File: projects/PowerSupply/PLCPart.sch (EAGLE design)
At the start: 30 parts, among them IC1 L7815CV, IC2 L7915CV, IC3 L7805CV, IC4 LM741P, IC5 LM741P, X1 SUPPLY-IN, X2 VCC-IN

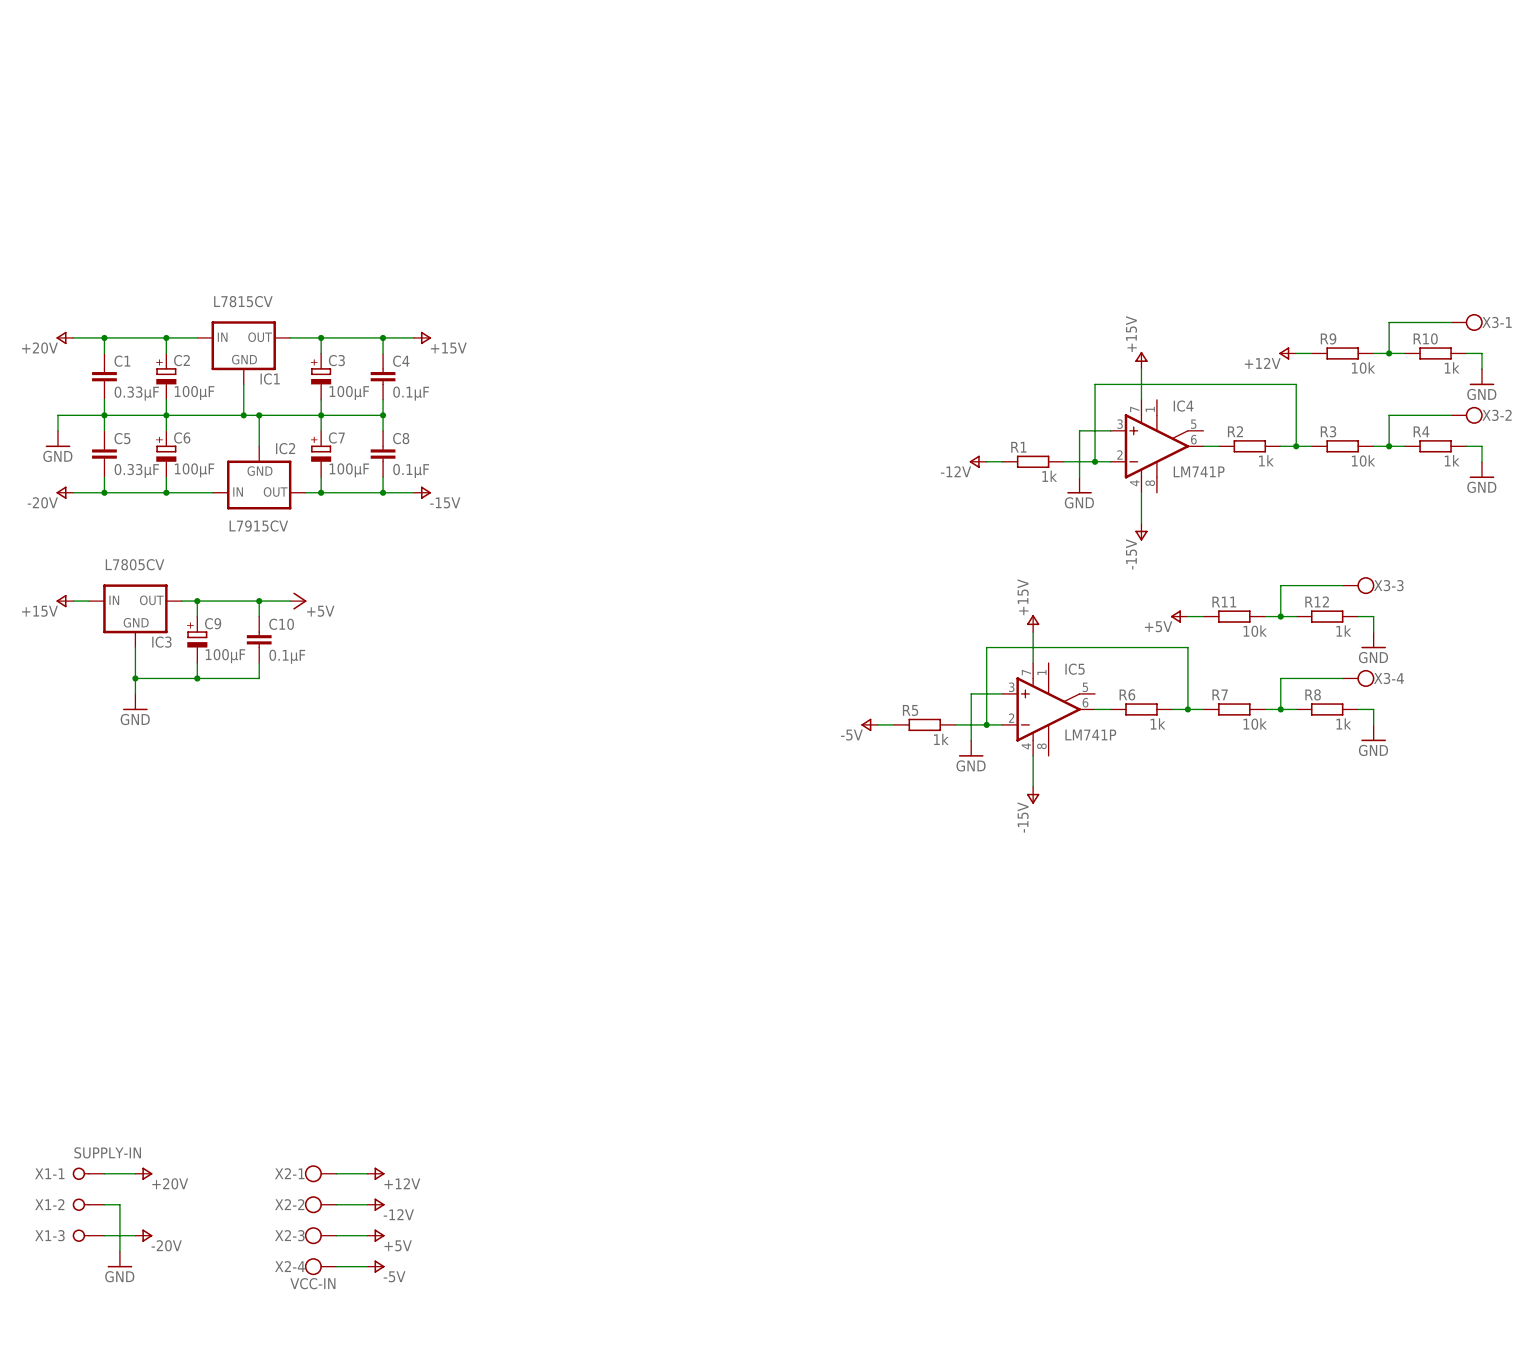
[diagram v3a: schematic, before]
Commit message: feat: plc part improved
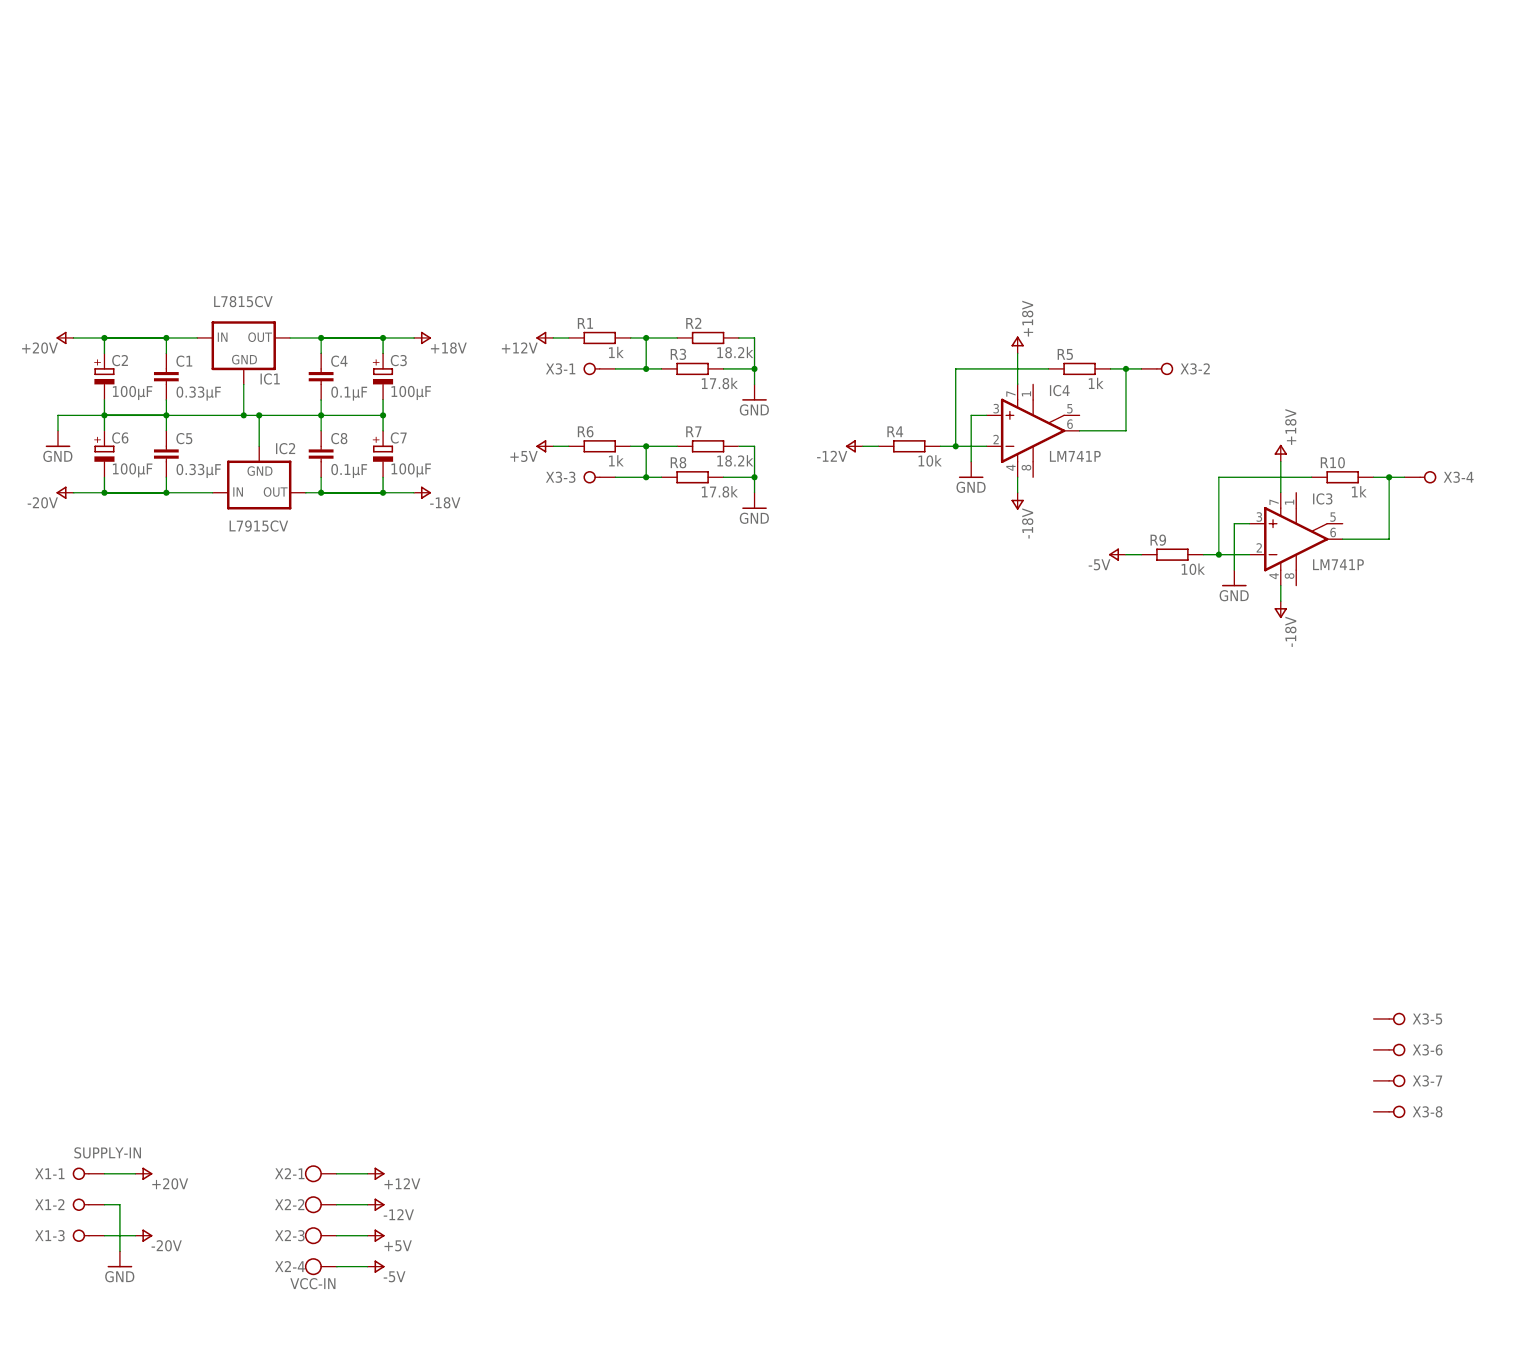
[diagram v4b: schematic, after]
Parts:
- removed C10: 0.1µF, rcl:C-EU050-024X044
- removed C9: 100µF, rcl:CPOL-EUE2.5-6
- removed IC5: LM741P, linear:LM741P
- removed R11: 10k, rcl:R-EU_0207/10
- removed R12: 1k, rcl:R-EU_0207/10
- IC3: value L7805CV -> LM741P; device v-reg:78XXS -> linear:LM741P
- R2: value 1k -> 18.2k
- R3: value 10k -> 17.8k
- R4: value 1k -> 10k
- R7: value 10k -> 18.2k
- R8: value 1k -> 17.8k
- X3: device con-wago-500:W237-4 -> con-wago-508:W237-08P
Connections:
- removed net +15V: C3.+, C4.1, IC1.OUT, IC3.IN, IC4.V+, IC5.V+
- removed net -15V: C7.-, C8.2, IC2.OUT, IC4.V-, IC5.V-
- removed net N$10: R11.2, R12.1, X3-3.KL
- removed net N$8: R10.1, R9.2, X3-1.KL
- new net +18V: C3.+, C4.1, IC1.OUT, IC3.V+, IC4.V+
- new net -18V: C7.-, C8.2, IC2.OUT, IC3.V-, IC4.V-
- net +12V: now also R1.1; no longer R9.1
- net +5V: now also R6.1; no longer C10.1, C9.+, IC3.OUT, R11.1
- net -12V: now also R4.1; no longer R1.1
- net -5V: now also R9.1; no longer R5.1
- net GND: now also IC3.+IN, R2.2, R3.2, R7.2; no longer C10.2, C9.-, IC3.GND, IC5.+IN, R10.2, R12.2, R4.2
- net N$1: now also R4.2, R5.1; no longer R1.2, R2.2, R3.1
- net N$2: now also IC4.OUT, R5.2; no longer R3.2, R4.1
- net N$3: now also IC3.-IN, R10.1, R9.2; no longer IC4.OUT, R2.1
- net N$4: now also R8.1, X3-3.KL; no longer IC5.-IN, R5.2
- net N$5: now also R1.2, R2.1, R3.1, X3-1.KL; no longer IC5.OUT, R6.1
- net N$6: now also IC3.OUT, R10.2; no longer R7.2, R8.1
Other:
- moved on the sheet: C1, C2, C3, C4, C5, C6, C7, C8, IC4, R1, R10, R2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

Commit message: feat: plc part small fixes applied
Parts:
- IC1: value L7815CV -> L7818CV
- IC2: value L7915CV -> L7918CV
- X1: value SUPPLY-IN -> MCU-PWR
- X2: value VCC-IN -> MCU-IN; device con-wago-500:W237-4 -> con-wago-508:W237-04P
- X3: value (none) -> MCU-OUT
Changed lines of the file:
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@@
 <parts>
 <part name="GND5" library="supply1" library_urn="urn:adsk.eagle:library:371" deviceset="GND" device=""/>
-<part name="X1" library="con-wago-508" library_urn="urn:adsk.eagle:library:196" deviceset="W237-03P" device="" package3d_urn="urn:adsk.eagle:package:10737/1" value="SUPPLY-IN"/>
+<part name="X1" library="con-wago-508" library_urn="urn:adsk.eagle:library:196" deviceset="W237-03P" device="" package3d_urn="urn:adsk.eagle:package:10737/1" value="MCU-PWR"/>
 <part name="P+4" library="bb84-supply" deviceset="+20V" device=""/>
 <part name="P-4" library="bb84-supply" deviceset="-20V" device=""/>
 <part name="FRAME1" library="frames" library_urn="urn:adsk.eagle:library:229" deviceset="A4L-LOC" device="" value="12VPart"/>
-<part name="IC2" library="v-reg" library_urn="urn:adsk.eagle:library:409" deviceset="79XXS" device="" package3d_urn="urn:adsk.eagle:package:30343/1" value="L7915CV"/>
-<part name="IC1" library="v-reg" library_urn="urn:adsk.eagle:library:409" deviceset="78XXS" device="" package3d_urn="urn:adsk.eagle:package:30342/1" value="L7815CV"/>
+<part name="IC2" library="v-reg" library_urn="urn:adsk.eagle:library:409" deviceset="79XXS" device="" package3d_urn="urn:adsk.eagle:package:30343/1" value="L7918CV"/>
+<part name="IC1" library="v-reg" library_urn="urn:adsk.eagle:library:409" deviceset="78XXS" device="" package3d_urn="urn:adsk.eagle:package:30342/1" value="L7818CV"/>
 <part name="P+1" library="bb84-supply" deviceset="+20V" device=""/>
 <part name="P-1" library="bb84-supply" deviceset="-20V" device=""/>
@@
 <part name="C6" library="rcl" library_urn="urn:adsk.eagle:library:334" deviceset="CPOL-EU" device="E2.5-6" package3d_urn="urn:adsk.eagle:package:23349/1" value="100µF"/>
 <part name="C7" library="rcl" library_urn="urn:adsk.eagle:library:334" deviceset="CPOL-EU" device="E2.5-6" package3d_urn="urn:adsk.eagle:package:23349/1" value="100µF"/>
-<part name="X2" library="con-wago-500" library_urn="urn:adsk.eagle:library:195" deviceset="W237-4" device="" package3d_urn="urn:adsk.eagle:package:10695/1" value="VCC-IN"/>
 <part name="P+6" library="bb84-supply" deviceset="+12V" device=""/>
 <part name="P-3" library="bb84-supply" deviceset="-12V" device=""/>
@@
 <part name="P+3" library="bb84-supply" deviceset="+18V" device=""/>
 <part name="P-6" library="bb84-supply" deviceset="-18V" device=""/>
-<part name="X3" library="con-wago-508" library_urn="urn:adsk.eagle:library:196" deviceset="W237-08P" device="" package3d_urn="urn:adsk.eagle:package:10738/1"/>
+<part name="X3" library="con-wago-508" library_urn="urn:adsk.eagle:library:196" deviceset="W237-08P" device="" package3d_urn="urn:adsk.eagle:package:10738/1" value="MCU-OUT"/>
 <part name="P+8" library="bb84-supply" deviceset="+12V" device=""/>
 <part name="R1" library="rcl" library_urn="urn:adsk.eagle:library:334" deviceset="R-EU_" device="0207/10" package3d_urn="urn:adsk.eagle:package:23491/2" value="1k"/>
@@
 <part name="P+9" library="bb84-supply" deviceset="+5V" device=""/>
 <part name="P-8" library="bb84-supply" deviceset="-5V" device=""/>
+<part name="X2" library="con-wago-508" library_urn="urn:adsk.eagle:library:196" deviceset="W237-04P" device="" package3d_urn="urn:adsk.eagle:package:10735/1" value="MCU-IN"/>
 </parts>
 <sheets>
@@
 <attribute name="VALUE" x="69.723" y="145.2626" size="1.778" layer="96"/>
 </instance>
-<instance part="X2" gate="-1" x="55.88" y="30.48" smashed="yes">
-<attribute name="NAME" x="55.88" y="31.369" size="1.778" layer="95" rot="R180"/>
-</instance>
-<instance part="X2" gate="-2" x="55.88" y="25.4" smashed="yes">
-<attribute name="NAME" x="55.88" y="26.289" size="1.778" layer="95" rot="R180"/>
-</instance>
-<instance part="X2" gate="-3" x="55.88" y="20.32" smashed="yes">
-<attribute name="NAME" x="55.88" y="21.209" size="1.778" layer="95" rot="R180"/>
-</instance>
-<instance part="X2" gate="-4" x="55.88" y="15.24" smashed="yes">
-<attribute name="VALUE" x="53.34" y="11.557" size="1.778" layer="96"/>
-<attribute name="NAME" x="55.88" y="16.129" size="1.778" layer="95" rot="R180"/>
-</instance>
 <instance part="P+6" gate="G$1" x="68.58" y="30.48" smashed="yes" rot="R270">
 <attribute name="VALUE" x="68.58" y="27.94" size="1.778" layer="96"/>
@@
 <instance part="P-8" gate="G$1" x="187.96" y="132.08" smashed="yes" rot="MR90">
 <attribute name="VALUE" x="187.96" y="129.54" size="1.778" layer="96" rot="MR0"/>
+</instance>
+<instance part="X2" gate="-1" x="55.88" y="30.48" smashed="yes">
+<attribute name="NAME" x="54.61" y="31.369" size="1.778" layer="95" rot="R180"/>
+</instance>
+<instance part="X2" gate="-2" x="55.88" y="25.4" smashed="yes">
+<attribute name="NAME" x="54.61" y="26.289" size="1.778" layer="95" rot="R180"/>
+</instance>
+<instance part="X2" gate="-3" x="55.88" y="20.32" smashed="yes">
+<attribute name="NAME" x="54.61" y="21.209" size="1.778" layer="95" rot="R180"/>
+</instance>
+<instance part="X2" gate="-4" x="55.88" y="15.24" smashed="yes">
+<attribute name="VALUE" x="55.88" y="33.02" size="1.778" layer="96"/>
+<attribute name="NAME" x="54.61" y="16.129" size="1.778" layer="95" rot="R180"/>
 </instance>
 </instances>
@@
 <net name="+5V" class="0">
 <segment>
-<pinref part="X2" gate="-3" pin="KL"/>
 <pinref part="P+7" gate="G$1" pin="+5V"/>
 <wire x1="60.96" y1="20.32" x2="66.04" y2="20.32" width="0.1524" layer="91"/>
+<pinref part="X2" gate="-3" pin="KL"/>
 </segment>
 <segment>
@@
 <net name="+12V" class="0">
 <segment>
-<pinref part="X2" gate="-1" pin="KL"/>
 <pinref part="P+6" gate="G$1" pin="+12V"/>
 <wire x1="60.96" y1="30.48" x2="66.04" y2="30.48" width="0.1524" layer="91"/>
+<pinref part="X2" gate="-1" pin="KL"/>
 </segment>
 <segment>
@@
 <segment>
 <pinref part="P-3" gate="G$1" pin="-12V"/>
+<wire x1="66.04" y1="25.4" x2="60.96" y2="25.4" width="0.1524" layer="91"/>
 <pinref part="X2" gate="-2" pin="KL"/>
-<wire x1="66.04" y1="25.4" x2="60.96" y2="25.4" width="0.1524" layer="91"/>
 </segment>
 <segment>
@@
 <segment>
 <pinref part="P-5" gate="G$1" pin="-5V"/>
+<wire x1="66.04" y1="15.24" x2="60.96" y2="15.24" width="0.1524" layer="91"/>
 <pinref part="X2" gate="-4" pin="KL"/>
-<wire x1="66.04" y1="15.24" x2="60.96" y2="15.24" width="0.1524" layer="91"/>
-</segment>
-<segment>
+</segment>
+<segment>

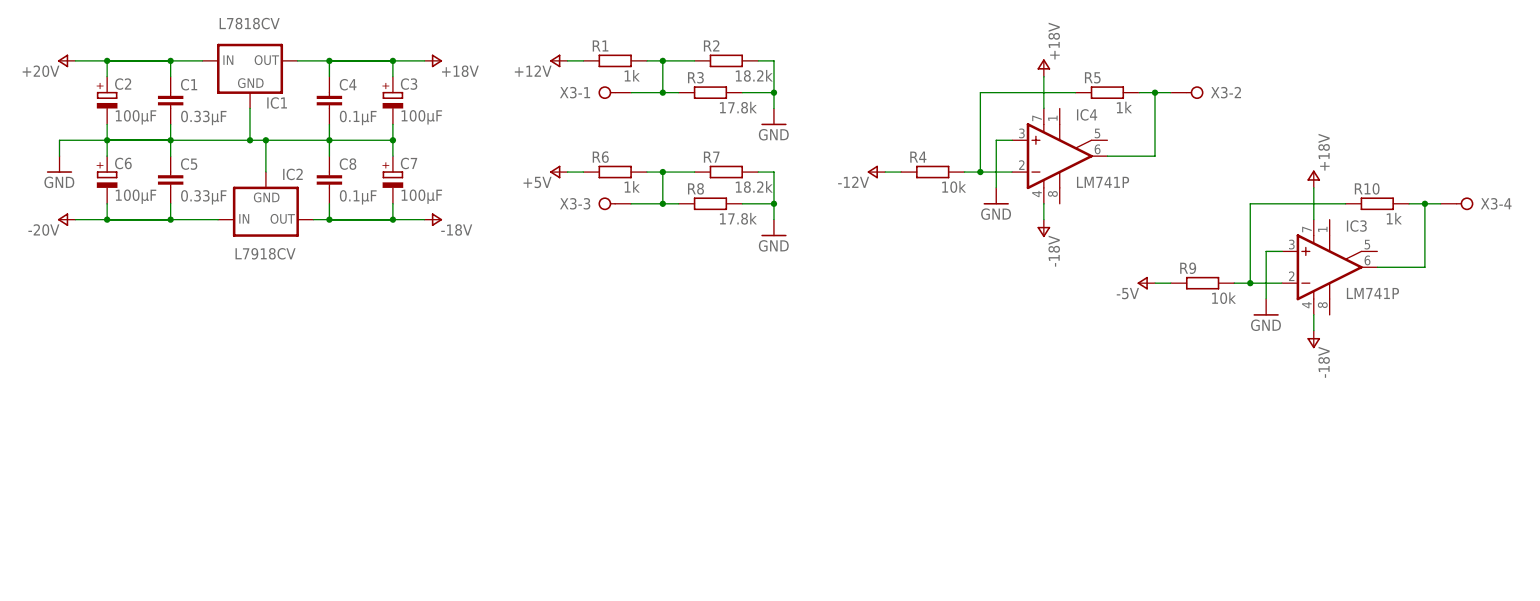
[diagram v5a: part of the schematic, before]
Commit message: feat: plc part 15 volts added
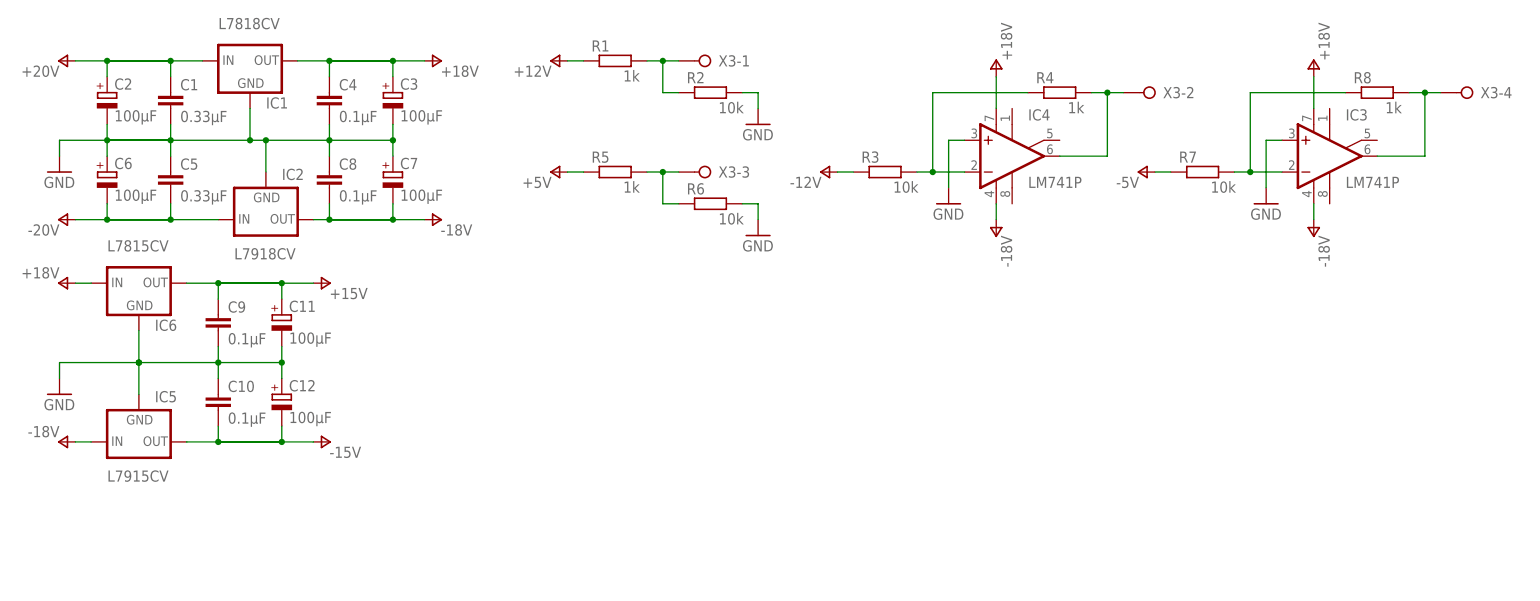
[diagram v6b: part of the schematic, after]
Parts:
- removed R10: 1k, rcl:R-EU_0207/10
- removed R9: 10k, rcl:R-EU_0207/10
- added C10, C9: 0.1µF, rcl:C-EU050-024X044
- added C11, C12: 100µF, rcl:CPOL-EUE2.5-6
- added IC5: L7915CV, v-reg:79XXS
- added IC6: L7815CV, v-reg:78XXS
- R2, R7: value 18.2k -> 10k
- R3: value 17.8k -> 10k
- R4: value 10k -> 1k
- R6: value 1k -> 10k
- R8: value 17.8k -> 1k
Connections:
- new net +15V: C11.+, C9.1, IC6.OUT
- new net -15V: C10.2, C12.-, IC5.OUT
- net +18V: now also IC6.IN
- net +5V: now also R5.1; no longer R6.1
- net -12V: now also R3.1; no longer R4.1
- net -18V: now also IC5.IN
- net -5V: now also R7.1; no longer R9.1
- net GND: now also C10.1, C11.-, C12.+, C9.2, IC5.GND, IC6.GND, R6.2; no longer R3.2, R7.2, R8.2
- net N$1: now also R3.2, R4.1; no longer R4.2, R5.1
- net N$2: now also R4.2; no longer R5.2
- net N$3: now also R7.2, R8.1; no longer R10.1, R9.2
- net N$4: now also R1.2, R2.1, X3-1.KL; no longer R6.2, R7.1, R8.1, X3-3.KL
- net N$5: now also R5.2, R6.1, X3-3.KL; no longer R1.2, R2.1, R3.1, X3-1.KL
- net N$6: now also R8.2; no longer R10.2
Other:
- moved on the sheet: IC3, IC4, R2, R3, R4, R5, R6, R7, R8, X3-1, X3-2, X3-3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
